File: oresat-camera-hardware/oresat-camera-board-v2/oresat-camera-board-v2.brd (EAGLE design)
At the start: 31.5 x 14 mm, 43 parts, among them J1 4-1734742-0, U1 AR0134CSSM00SPCA0, U2 TPS70618DRVR, U3 TPS71928-28DRVT, U4 TPS71928-28DRVT, X1 KC2520B27.0000C10E00

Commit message: more cleanup
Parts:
- J1: value 4-1734742-0 -> 3-1734742-6; device J-TEConnectivity-4-1734742-0:TE_4-1734742-0 -> J-TEConnectivity-3-1734742-6 :TE_3-1734742-6
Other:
- board text added: "MAKE SURE FFC CONNECTOR IS CORRECT ORIENTATION! CONTACTS MUST BE ON TOP OF CONNECTOR TO MATE WITH OCTAVO CARD. MEASURE TWICE CUT ONCE!!!!"

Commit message: made a few minor adjustments when I was making the BOMs
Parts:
- R5: value 10K -> 10k
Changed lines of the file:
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@@
 <?xml version="1.0" encoding="utf-8"?>
 <!DOCTYPE eagle SYSTEM "eagle.dtd">
-<eagle version="9.4.2">
+<eagle version="9.5.0">
 <drawing>
 <settings>
@@
 <attribute name="VALUE" x="20.7375" y="13.375" size="0.8" layer="28" font="vector" ratio="15" rot="MR270"/>
 </element>
-<element name="R5" library="oresat-rcl" package=".0402-B-NOSILK" value="10K" x="24" y="6.5" smashed="yes" rot="MR90">
+<element name="R5" library="oresat-rcl" package=".0402-B-NOSILK" value="10k" x="24" y="6.5" smashed="yes" rot="MR90">
 <attribute name="NAME" x="23.8" y="7.5125" size="0.5" layer="26" font="vector" ratio="15" rot="MR90"/>
 <attribute name="NAME" x="24" y="6.5" size="0.2" layer="34" ratio="15" rot="MR90" align="center"/>

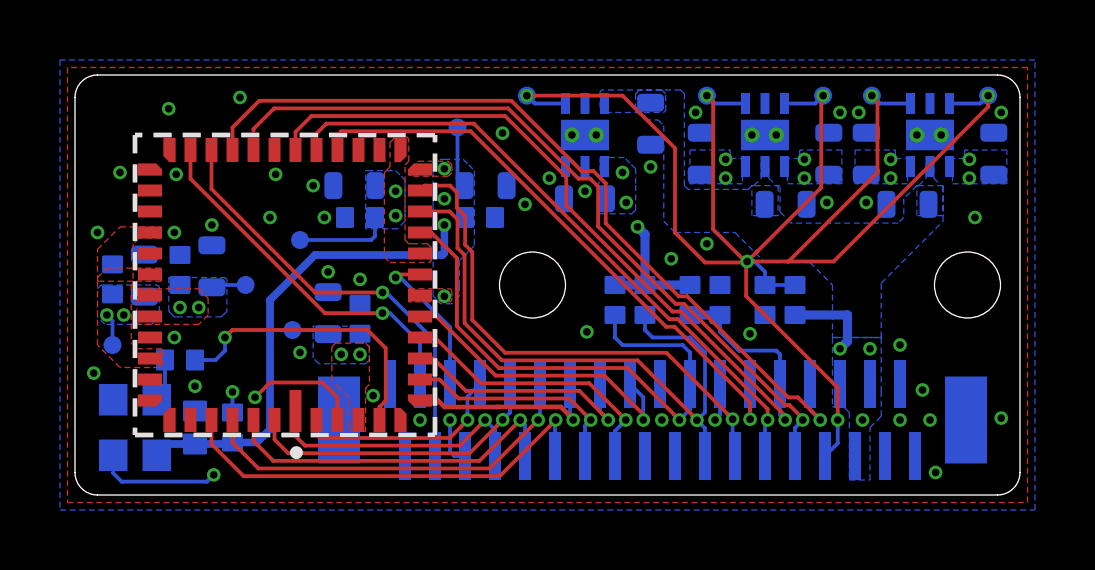
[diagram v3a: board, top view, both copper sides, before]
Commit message: mostly finished implementing v0 changes, but have a few more to go
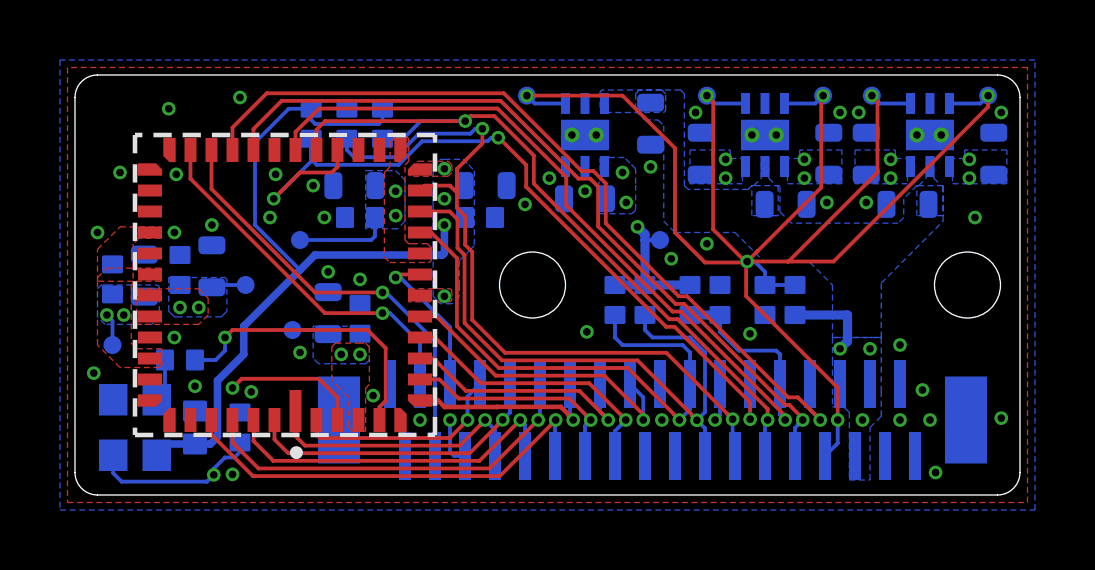
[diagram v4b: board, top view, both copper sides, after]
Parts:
- removed R1: 10k, oresat-rcl:.0402-B
- added R10, R11, R12, R9: 10k, oresat-rcl:.0402-B
- moved TP8 7.72 mm to (19.5, 8.50)
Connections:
- net !OE: now also R11.1
- net !RESET: now also R9.2
- net CLK_EN: now also R12.2; no longer R1.1
- net GND: now also R12.1, R9.1
- net STANDBY: now also R10.1
- net VDD_IO: now also R10.2, R11.2; no longer R1.2
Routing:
- net VDD_IO: track 34.0 -> 42.0 mm
- net !RESET: track 17.2 -> 25.0 mm, vias 1 -> 2
- net STANDBY: track 19.8 -> 27.2 mm, vias 1 -> 3
- net !OE: track 21.3 -> 25.1 mm, vias 1 -> 2
- net D6: track 12.8 -> 14.8 mm
- net CLK_EN: track 25.6 -> 24.7 mm, vias 3 -> 2
